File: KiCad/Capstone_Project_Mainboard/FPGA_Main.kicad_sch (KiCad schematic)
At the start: 1 part, among them J3 Xilinx Cable Header

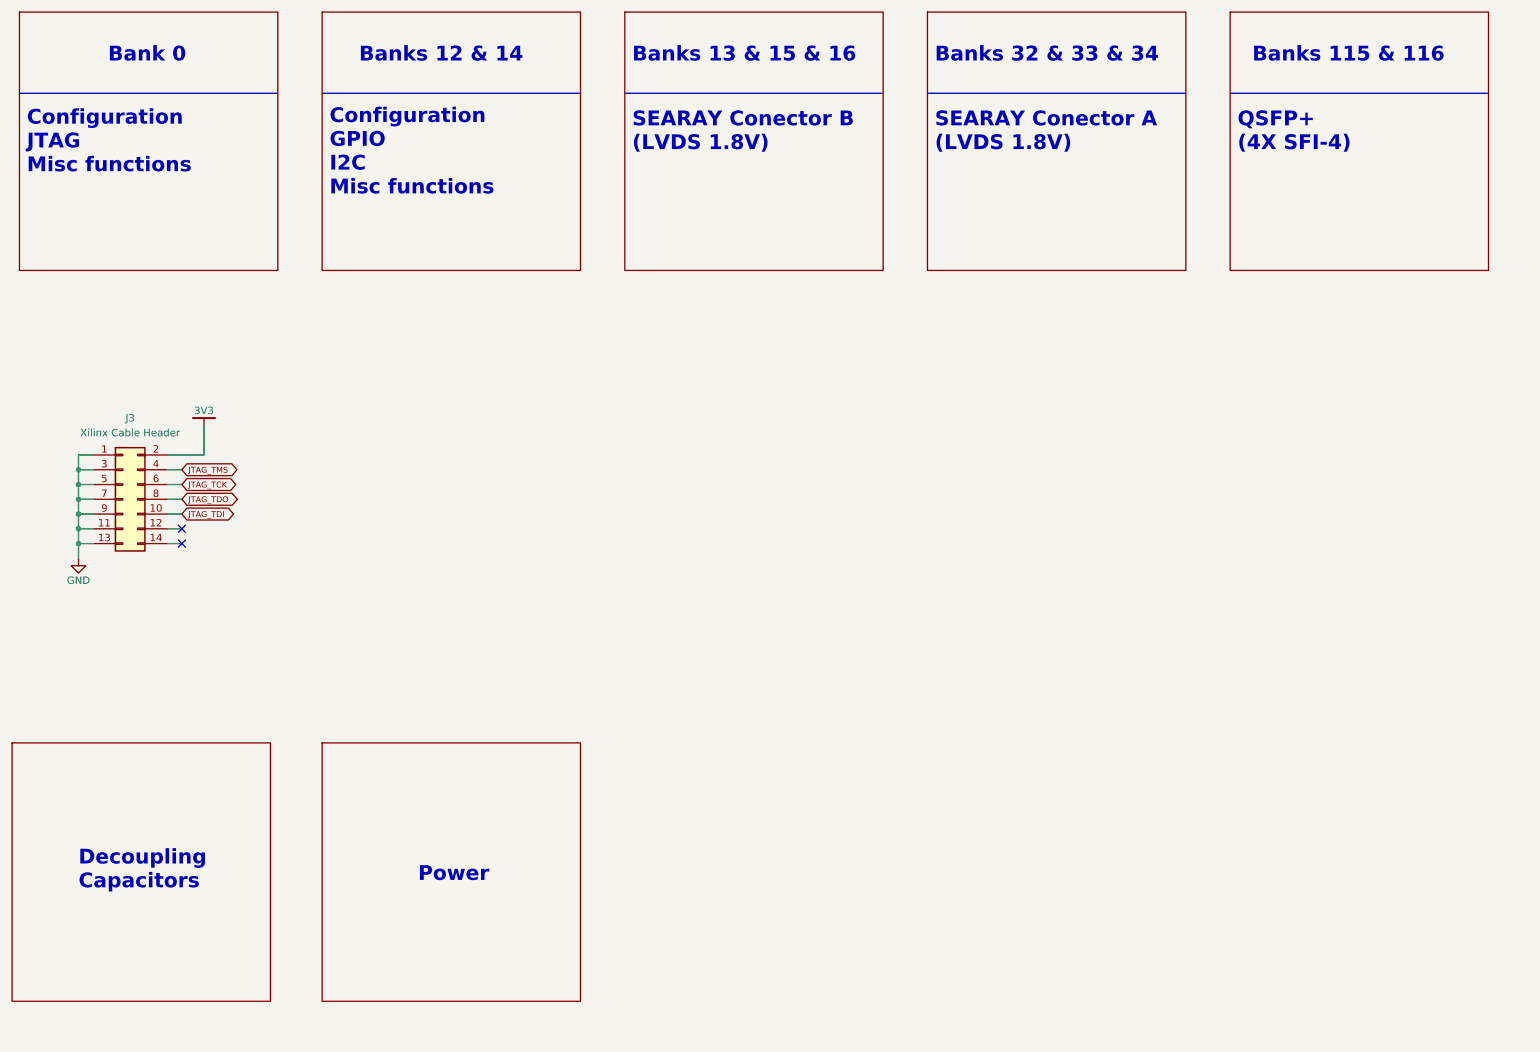
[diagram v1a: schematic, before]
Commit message: Core non-power parts defined
Most major non-power components added to KiCad project
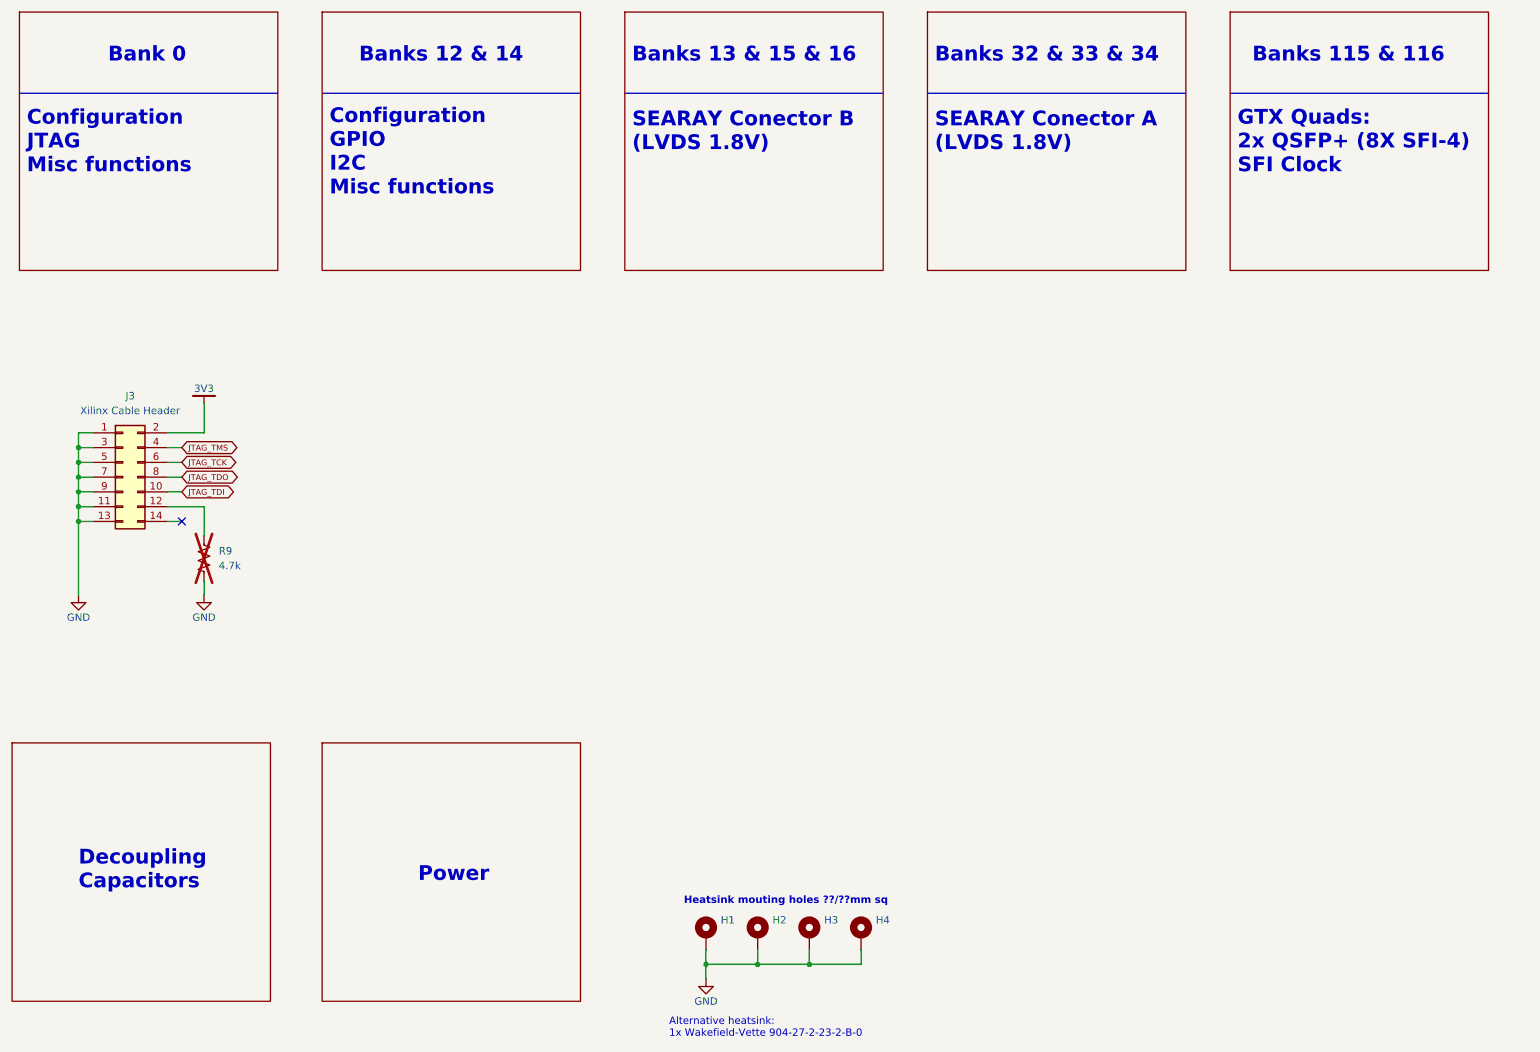
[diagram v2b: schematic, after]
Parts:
- added H1, H2, H3, H4: Heatsink MH, MountingHole:MountingHole_2.5mm_Pad, symbol Mechanical:MountingHole_Pad
- added R9: 4.7k, Resistor_SMD:R_0402_1005Metric, symbol Device:R_US
- J3: footprint (none) -> Capstone_Library:0878321420; Part Number (none) -> 0878321420
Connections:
- net GND: now also H1.1, H2.1, H3.1, H4.1, R9.2
- net at J3.12 (Pin_12): now also R9.1
- no-connect marks 2 -> 1
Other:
- note added: "Alternative heatsink: 1x Wakefield-Vette 904-27-2-23-2-B-0"
- note added: "GTX Quads: 2x QSFP+ (8X SFI-4) SFI Clock"
- note added: "Heatsink mouting holes ??/??mm sq"
- note removed: "QSFP+ (4X SFI-4)"
- moved on the sheet: J3
